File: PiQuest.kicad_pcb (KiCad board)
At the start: 2 copper layers, 80 x 100 mm, 17 parts, among them Q1 FS8205A_C2830320, SW1 SW_Omron_B3FS, SW10 SW_Omron_B3FS, SW2 SW_Omron_B3FS, SW3 SW_Omron_B3FS, SW4 SW_Omron_B3FS, SW5 SW_Omron_B3FS, SW6 SW_Omron_B3FS, SW7 SW_Omron_B3FS, SW8 SW_Omron_B3FS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

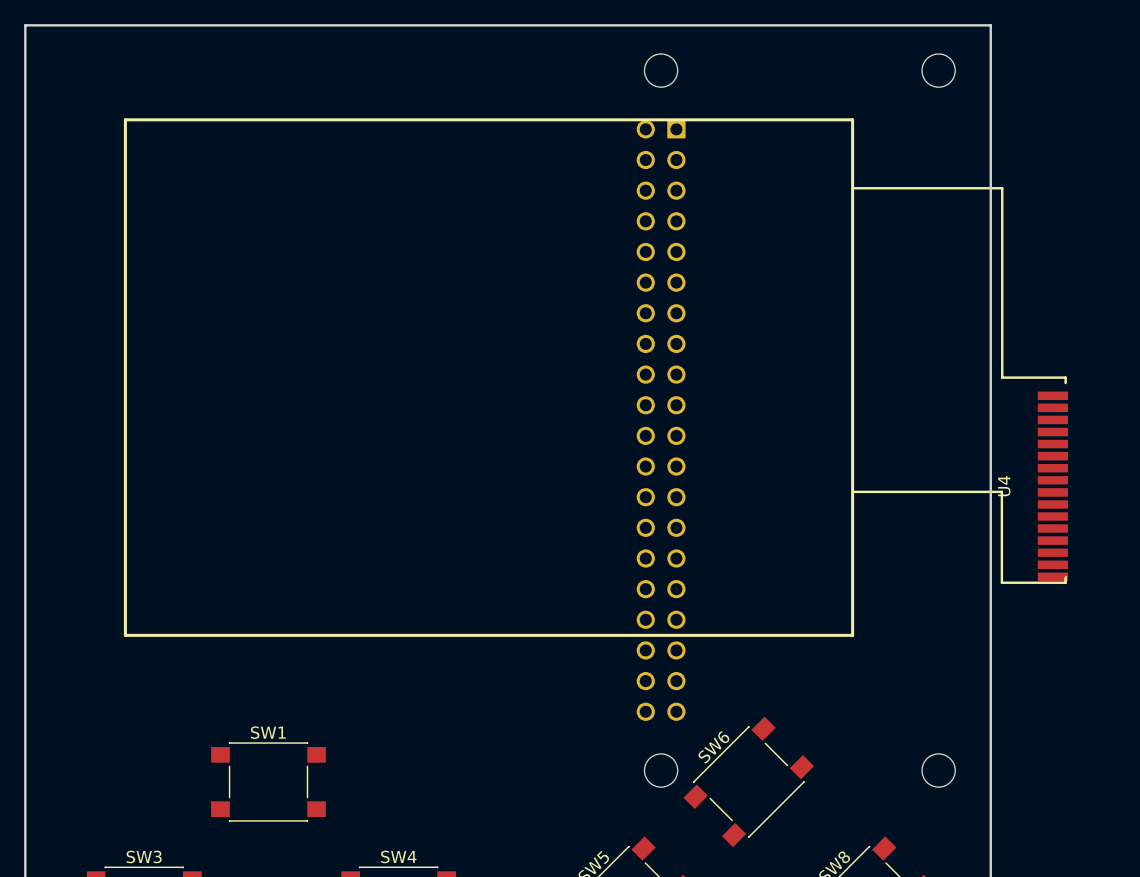
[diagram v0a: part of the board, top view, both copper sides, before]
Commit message: added buttons
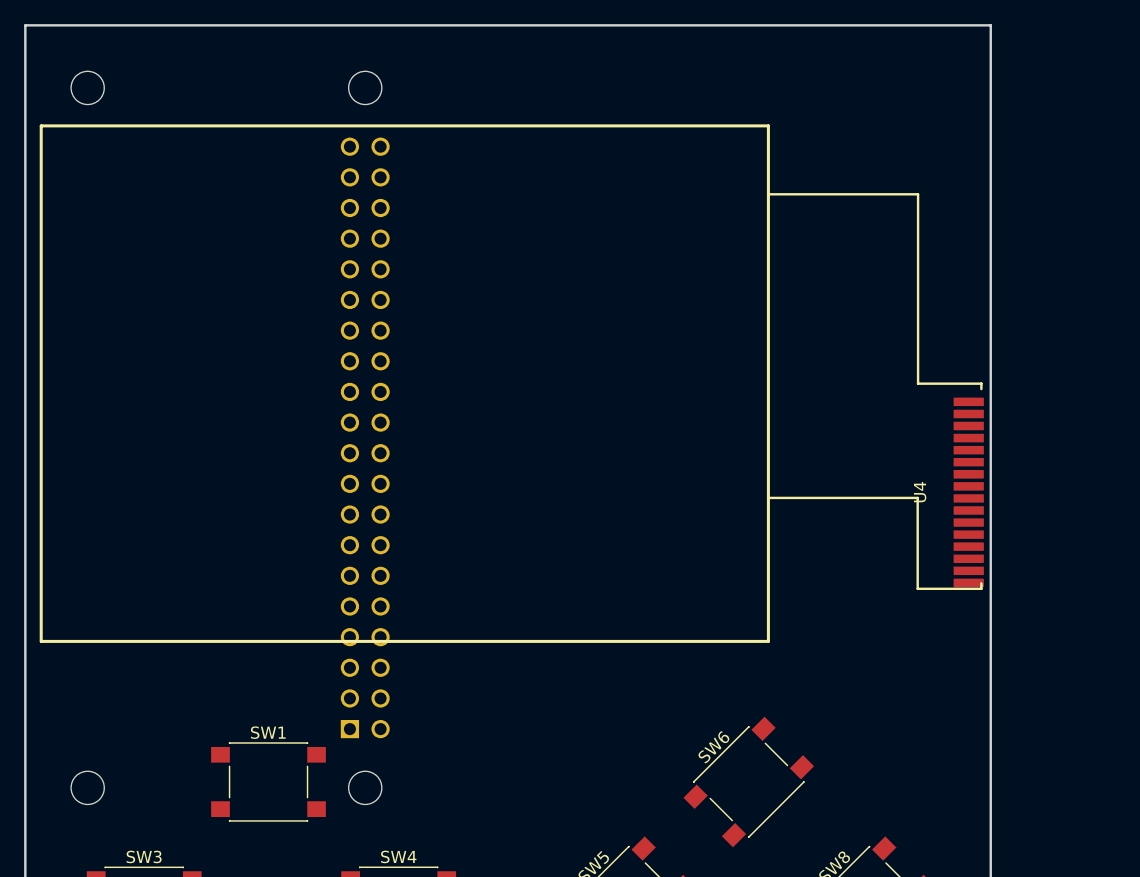
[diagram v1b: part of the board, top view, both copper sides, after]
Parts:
- moved A1 24.6 mm to (108.9, 75.4), turned to 90 degrees
- moved U4 6.99 mm to (158.9, 79.9)

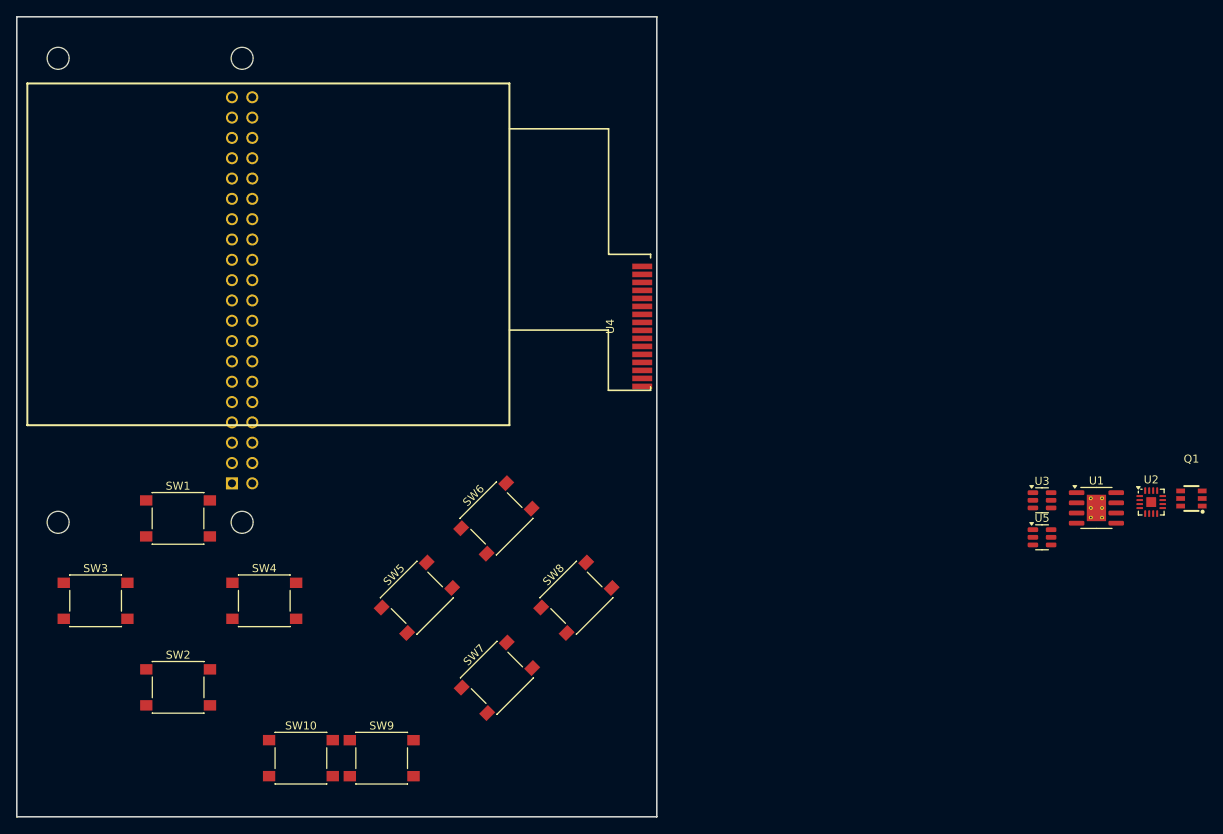
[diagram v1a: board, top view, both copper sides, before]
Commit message: fixed lcd footprint
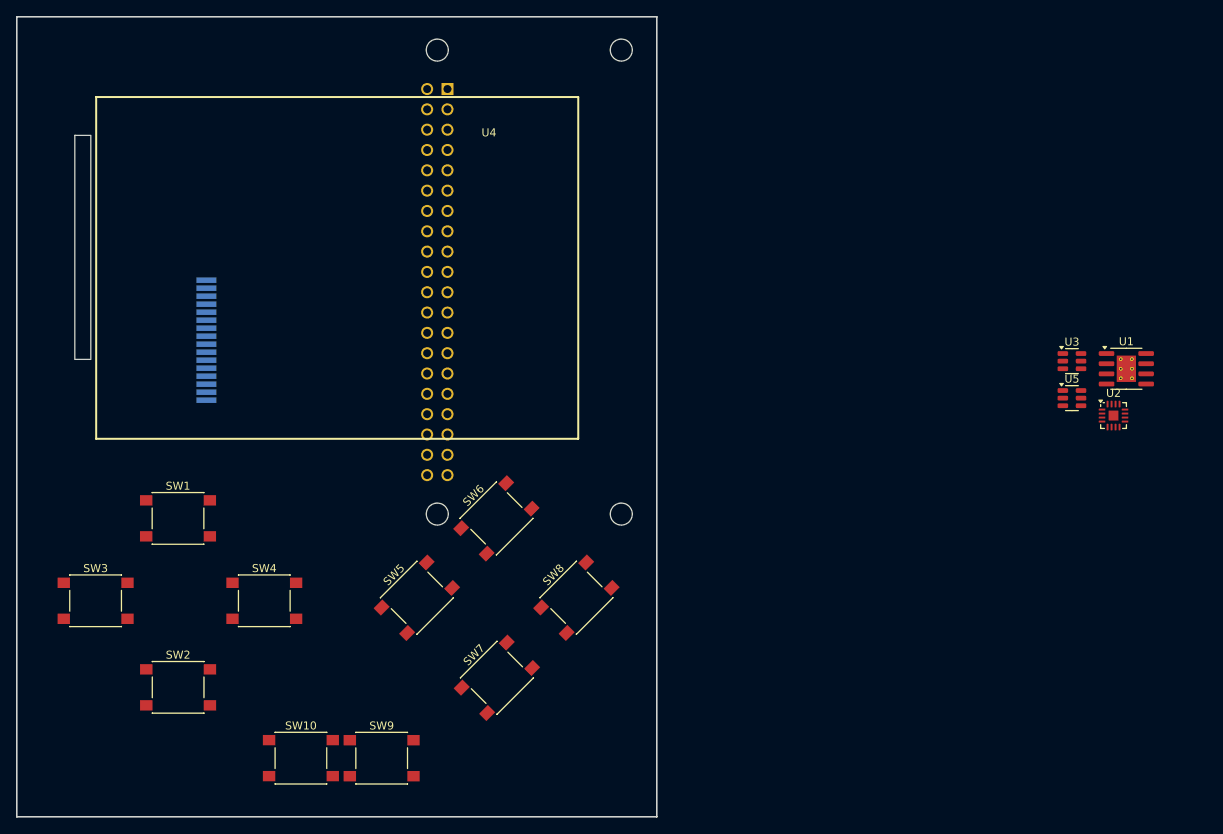
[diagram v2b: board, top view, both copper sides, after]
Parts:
- removed Q1: FS8205A_C2830320, easyeda2kicad:SOT-23-6_L2.9-W1.6-P0.95-LS2.8-BR
- U4: footprint easyeda2kicad:LCD-SMD_HS24CG003-ARX -> easyeda2kicad:lcd
- moved U4 29.8 mm to (150.9, 51.2), turned to 0 degrees
- moved A1 24.4 mm to (133.3, 74.4), turned to -90 degrees
- moved U1 17.8 mm to (219.4, 85.2)
- moved U3 17.8 mm to (212.6, 84.2)
- moved U5 17.8 mm to (212.6, 88.9)
- moved U2 11.8 mm to (217.8, 91.0)

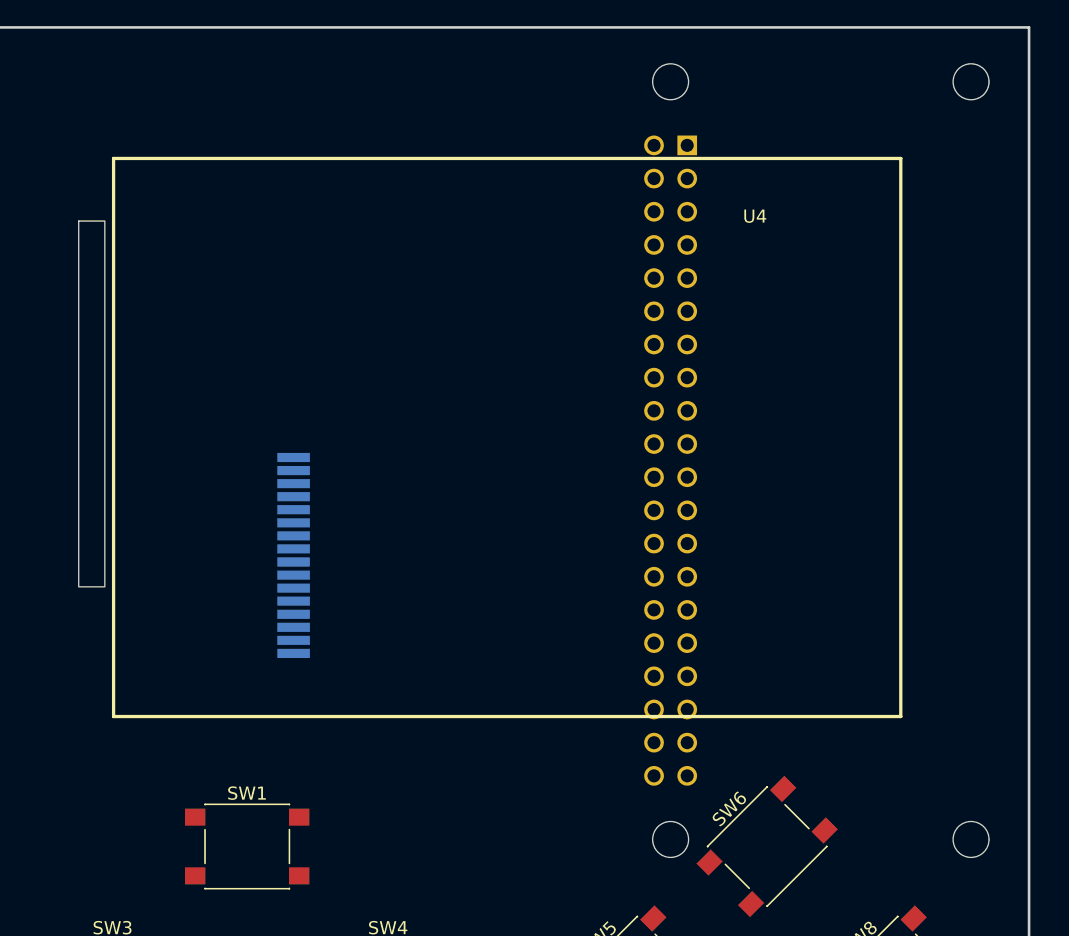
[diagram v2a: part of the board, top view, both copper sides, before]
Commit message: fixed display
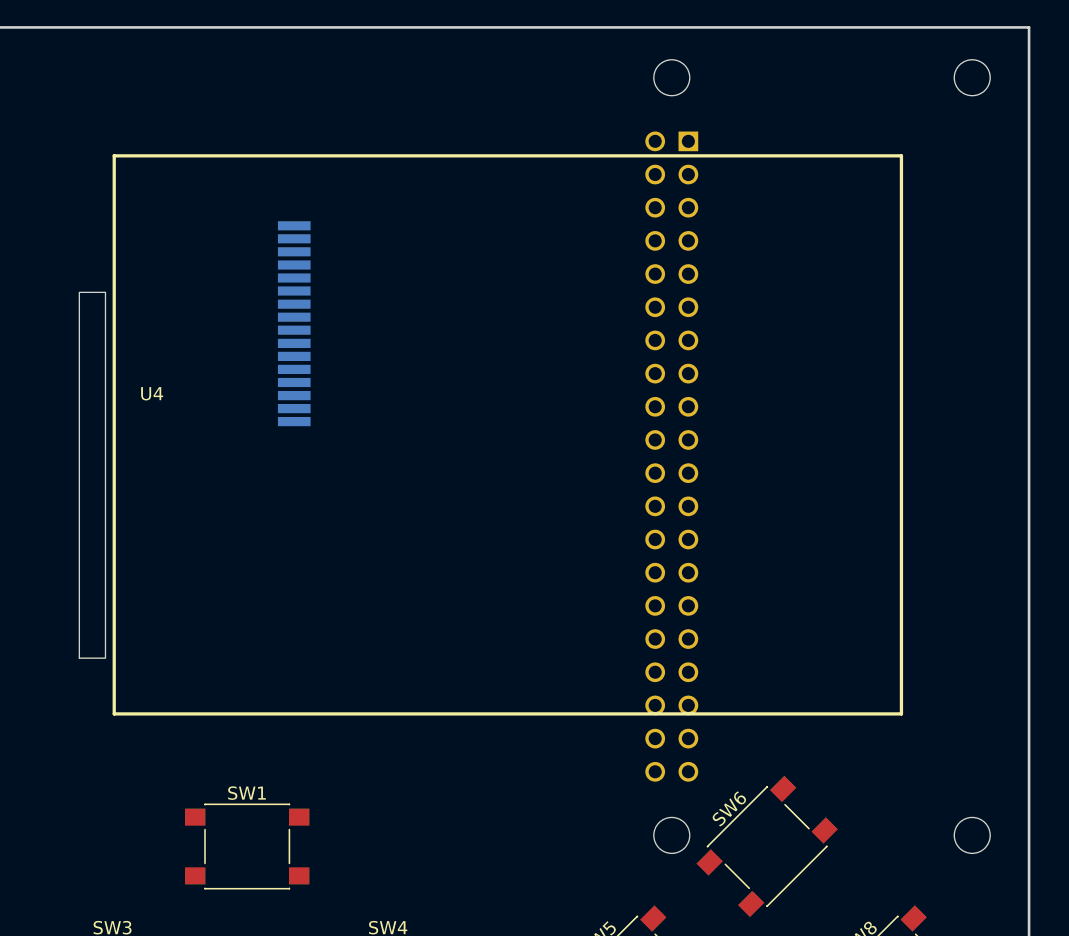
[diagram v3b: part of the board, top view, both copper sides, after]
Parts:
- moved A1 0.32 mm to (133.4, 74.0)
- moved U4 0.21 mm to (150.9, 51.0)
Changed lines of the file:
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@@
 	(footprint "easyeda2kicad:lcd"
 		(layer "F.Cu")
-		(at 150.9 51.22)
+		(at 150.95 51.02)
 		(property "Reference" "U4"
-			(at -11.13 4.46 0)
+			(at -57.35 18.25 0)
 			(unlocked yes)
 			(layer "F.SilkS")
@@
 		)
 		(property "Value" "HS24CG003-ARX"
-			(at -11.13 5.96 0)
+			(at -57.35 19.75 0)
 			(unlocked yes)
 			(layer "F.Fab")
@@
 		)
 		(fp_line
-			(start -50.64 38.39)
-			(end -50.64 30.86)
+			(start -51.14 20.44)
+			(end -47.99 20.38)
+			(stroke
+				(width 0.1)
+				(type default)
+			)
+			(layer "B.SilkS")
+		)
+		(fp_line
+			(start -50.64 4.87)
+			(end -50.64 12.4)
 			(stroke
 				(width 0.2)
@@
 		)
 		(fp_line
-			(start -50.52 30.88)
-			(end -62.72 30.89)
+			(start -50.52 12.38)
+			(end -62.72 12.37)
 			(stroke
 				(width 0.2)
@@
 		)
 		(fp_line
-			(start -50.19 5.19)
-			(end -62.59 5.19)
+			(start -50.19 22.38)
+			(end -50.19 38.07)
 			(stroke
 				(width 0.2)
@@
 		)
 		(fp_line
-			(start -50.19 20.88)
-			(end -50.19 5.19)
+			(start -50.19 38.07)
+			(end -62.59 38.07)
 			(stroke
 				(width 0.2)
@@
 		)
 		(fp_line
-			(start -45.4 21.39)
-			(end -50.65 21.39)
+			(start -45.4 21.42)
+			(end -45.4 21.87)
 			(stroke
 				(width 0.2)
@@
 		)
 		(fp_line
-			(start -45.4 21.84)
-			(end -45.4 21.39)
+			(start -45.4 21.87)
+			(end -50.65 21.87)
 			(stroke
 				(width 0.2)
@@
 		)
 		(fp_line
-			(start -45.36 37.94)
-			(end -45.36 38.39)
+			(start -45.36 4.87)
+			(end -50.64 4.87)
 			(stroke
 				(width 0.2)
@@
 		)
 		(fp_line
-			(start -45.36 38.39)
-			(end -50.64 38.39)
+			(start -45.36 5.32)
+			(end -45.36 4.87)
 			(stroke
 				(width 0.2)
@@
 		)
 		(fp_rect
-			(start -62.9 4.8)
-			(end -60.9 32.8)
+			(start -62.9 38.46)
+			(end -60.9 10.46)
 			(stroke
 				(width 0.05)
@@
 		)
 		(fp_circle
-			(center -47.9 21.39)
-			(end -47.9 21.36)
+			(center -47.9 21.87)
+			(end -47.9 21.9)
 			(stroke
 				(width 0.06)
@@
 		)
 		(fp_text user "${REFERENCE}"
-			(at -12.7 9.79 270)
+			(at -48.365224 13.68 270)
 			(layer "B.Fab")
 			(effects
@@
 		)
 		(fp_text user "${REFERENCE}"
-			(at 15.1 0.95 0)
+			(at -57.35 21.25 0)
 			(unlocked yes)
 			(layer "F.Fab")
@@
 			(layer "User.1")
 			(pts
-				(xy 90.67 93.95) (xy 105.76 93.95)
+				(xy 90.72 93.75) (xy 105.81 93.75)
 			)
 			(height -30.2)
@@
 			)
 			(gr_text "15.09"
-				(at 98.215 62.6 0)
+				(at 98.265 62.4 0)
 				(layer "User.1")
 				(effects
@@
 		)
 		(pad "1" smd rect
-			(at -46.45 22.9 90)
+			(at -46.45 20.36 270)
 			(size 0.7 2.5)
 			(layers "B.Cu" "B.Mask" "B.Paste")
@@
 		)
 		(pad "2" smd rect
-			(at -46.45 23.9 90)
+			(at -46.45 19.36 270)
 			(size 0.7 2.5)
 			(layers "B.Cu" "B.Mask" "B.Paste")
@@
 		)
 		(pad "3" smd rect
-			(at -46.45 24.9 90)
+			(at -46.45 18.36 270)
 			(size 0.7 2.5)
 			(layers "B.Cu" "B.Mask" "B.Paste")
@@
 		)
 		(pad "4" smd rect
-			(at -46.45 25.9 90)
+			(at -46.45 17.36 270)
 			(size 0.7 2.5)
 			(layers "B.Cu" "B.Mask" "B.Paste")
@@
 		)
 		(pad "5" smd rect
-			(at -46.45 26.9 90)
+			(at -46.45 16.36 270)
 			(size 0.7 2.5)
 			(layers "B.Cu" "B.Mask" "B.Paste")
@@
 		)
 		(pad "6" smd rect
-			(at -46.45 27.9 90)
+			(at -46.45 15.36 270)
 			(size 0.7 2.5)
 			(layers "B.Cu" "B.Mask" "B.Paste")
@@
 		)
 		(pad "7" smd rect
-			(at -46.45 28.9 90)
+			(at -46.45 14.36 270)
 			(size 0.7 2.5)
 			(layers "B.Cu" "B.Mask" "B.Paste")
@@
 		)
 		(pad "8" smd rect
-			(at -46.45 29.9 90)
+			(at -46.45 13.36 270)
 			(size 0.7 2.5)
 			(layers "B.Cu" "B.Mask" "B.Paste")
@@
 		)
 		(pad "9" smd rect
-			(at -46.45 30.9 90)
+			(at -46.45 12.36 270)
 			(size 0.7 2.5)
 			(layers "B.Cu" "B.Mask" "B.Paste")
@@
 		)
 		(pad "10" smd rect
-			(at -46.45 31.9 90)
+			(at -46.45 11.36 270)
 			(size 0.7 2.5)
 			(layers "B.Cu" "B.Mask" "B.Paste")
@@
 		)
 		(pad "11" smd rect
-			(at -46.45 32.9 90)
+			(at -46.45 10.36 270)
 			(size 0.7 2.5)
 			(layers "B.Cu" "B.Mask" "B.Paste")
@@
 		)
 		(pad "12" smd rect
-			(at -46.45 33.9 90)
+			(at -46.45 9.36 270)
 			(size 0.7 2.5)
 			(layers "B.Cu" "B.Mask" "B.Paste")
@@
 		)
 		(pad "13" smd rect
-			(at -46.45 34.9 90)
+			(at -46.45 8.36 270)
 			(size 0.7 2.5)
 			(layers "B.Cu" "B.Mask" "B.Paste")
@@
 		)
 		(pad "14" smd rect
-			(at -46.45 35.9 90)
+			(at -46.45 7.36 270)
 			(size 0.7 2.5)
 			(layers "B.Cu" "B.Mask" "B.Paste")
@@
 		)
 		(pad "15" smd rect
-			(at -46.45 36.9 90)
+			(at -46.45 6.36 270)
 			(size 0.7 2.5)
 			(layers "B.Cu" "B.Mask" "B.Paste")
@@
 		)
 		(pad "16" smd rect
-			(at -46.45 37.9 90)
+			(at -46.45 5.36 270)
 			(size 0.7 2.5)
 			(layers "B.Cu" "B.Mask" "B.Paste")
@@
 		)
 		(embedded_fonts no)
+		(model "C:/Users/aniru/Documents/KiCad/easyeda2kicad/easyeda2kicad.3dshapes/LCD-SMD_HS24CG003-ARX.step"
+			(hide yes)
+			(offset
+				(xyz -30 -21.5 0)
+			)
+			(scale
+				(xyz 1 1 1)
+			)
+			(rotate
+				(xyz -0 -0 90)
+			)
+		)
+		(model "C:/Users/aniru/Documents/KiCad/easyeda2kicad/easyeda2kicad.3dshapes/LCD-SMD_HS24CG003-ARX.wrl"
+			(offset
+				(xyz -30 -21.5 0)
+			)
+			(scale
+				(xyz 1 1 1)
+			)
+			(rotate
+				(xyz -0 -0 90)
+			)
+		)
 	)
 	(footprint "Package_TO_SOT_SMD:SOT-23-6"
@@
 	(footprint "RASPBERRYPI-ZERO:RASPBERRYPI-ZERO_RPI-ZERO"
 		(layer "B.Cu")
-		(at 133.31 74.36 -90)
+		(at 133.4 74.05 -90)
 		(descr "Raspberry Pi board model B+, full outline with position of big connectors &amp; drill holes")
 		(property "Reference" "A1"
@@
 	)
 	(gr_line
-		(start 136.15 51.02)
-		(end 136.15 41.15)
-		(stroke
-			(width 0.1)
-			(type solid)
-		)
-		(layer "User.1")
-	)
-	(gr_line
 		(start 130.7592 113.8174)
 		(end 140.716 103.8606)
@@
 	)
 	(gr_line
-		(start 150.95 51.23)
-		(end 160.82 51.23)
+		(start 150.95 51.02)
+		(end 160.82 51.02)
 		(stroke
 			(width 0.1)
@@
 		)
 		(layer "User.1")
+	)
+	(gr_line
+		(start 150.95 51.02)
+		(end 150.95 41.15)
+		(stroke
+			(width 0.1)
+			(type solid)
+		)
+		(layer "User.1")
